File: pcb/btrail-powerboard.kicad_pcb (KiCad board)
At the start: 2 copper layers, 33.5 x 27.5 mm, 10 parts, among them J1 RJ45, Q1 BC328, Q2 BC328, U2 XL1509-5.0

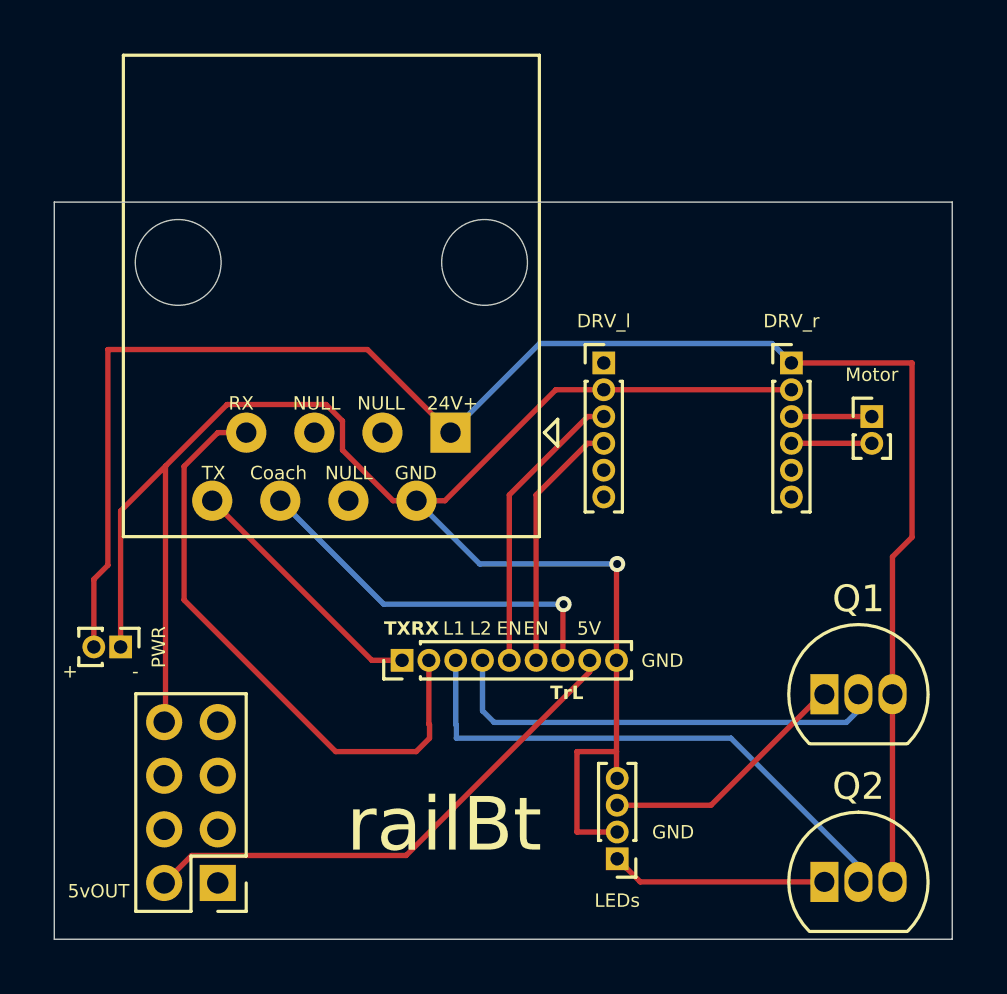
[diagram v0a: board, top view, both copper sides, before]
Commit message: Update pcb with symmetrical pin layout on RJ45 jack
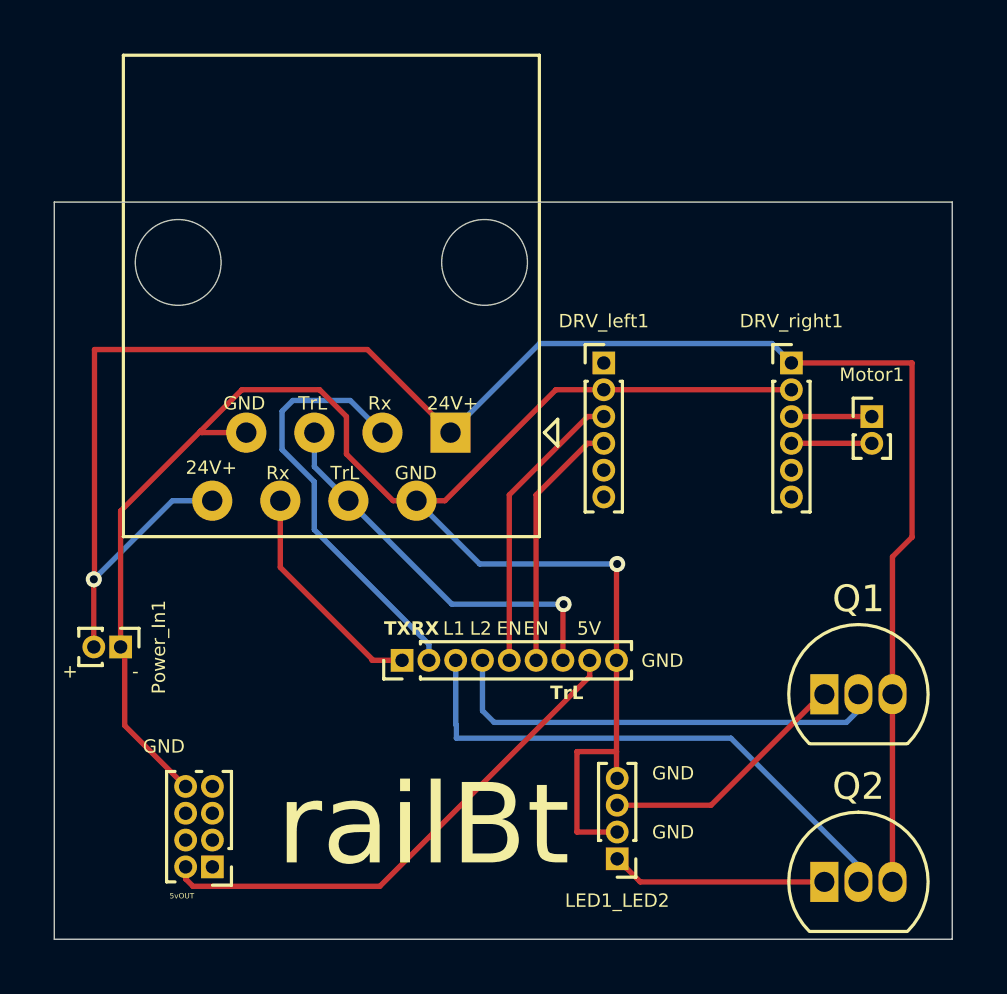
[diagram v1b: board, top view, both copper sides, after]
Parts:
- J1: value RJ45 -> RJ45 Shielded
- U2: footprint Connector_PinHeader_2.00mm:PinHeader_2x04_P2.00mm_Vertical -> Connector_PinHeader_1.00mm:PinHeader_2x04_P1.00mm_Vertical
- moved U2 0.63 mm to (197.4, 46.8)
- renumbered DRV_l to DRV_left1, DRV_r to DRV_right1, ESP32 to ESP32_jack1, LEDs to LED1_LED2, Motor to Motor1, PWR to Power_In1
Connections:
- J1 pad 3: unconnected-(J1-Pad3) -> Net-(ESP32_jack1-Pin_2)
- J1 pad 4: unconnected-(J1-Pad4) -> Net-(ESP32_jack1-Pin_7)
- J1 pad 5: unconnected-(J1-Pad5) -> Net-(ESP32_jack1-Pin_7)
- J1 pad 6: Net-(ESP32_jack1-Pin_7) -> Net-(ESP32_jack1-Pin_1)
- J1 pad 7: Net-(ESP32_jack1-Pin_2) -> Net-(DRV_left1-Pin_2)
- J1 pad 8: Net-(ESP32_jack1-Pin_1) -> Net-(DRV_right1-Pin_1)
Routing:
- net Net-(ESP32_jack1-Pin_2): track 22.4 -> 16.0 mm
- net Net-(DRV_right1-Pin_1): track 63.9 -> 69.9 mm, vias 0 -> 1
- net Net-(ESP32_jack1-Pin_1): track 9.55 -> 8.52 mm
- net Net-(DRV_left1-Pin_2): track 67.6 -> 66.6 mm
- net Net-(ESP32_jack1-Pin_7): track 14.3 -> 14.8 mm
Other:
- board text added: "Rx"
- board text removed: "Coach"
- board text removed: "NULL"
